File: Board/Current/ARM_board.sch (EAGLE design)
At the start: 168 parts, among them IC3 STM32F437VI, IC4 LM358DT, J1 USART/I2C, J10 ANALOG, J11 DGND, J12 DPWR, J13 DIGITAL, J14 SGND, J15 SPWR, J16 SERVO, J2 I2C2/USART3, J3 USART2, J5 SPI, J6 Bluesmirf, J7 SWD, J8 AGND, J9 APWR, Q1 STL4P2UH7, Q2 2STR1230, SW1 SW, U1 LSM330DLC, U10 BAV99, U11 BAV99, U12 USBLC6-2, U13 USBLC6-2, U14 STMPS2171MTR, U15 MC74HC164, U17 ?, U18 ?, U19 ?, U20 ?, U3 NC7SZU04, U4 L6206Q, U5 L6206Q, U6 SI7617, U7 SI7617, U8 SI7617, U9 SI7617, Y2 8MHz

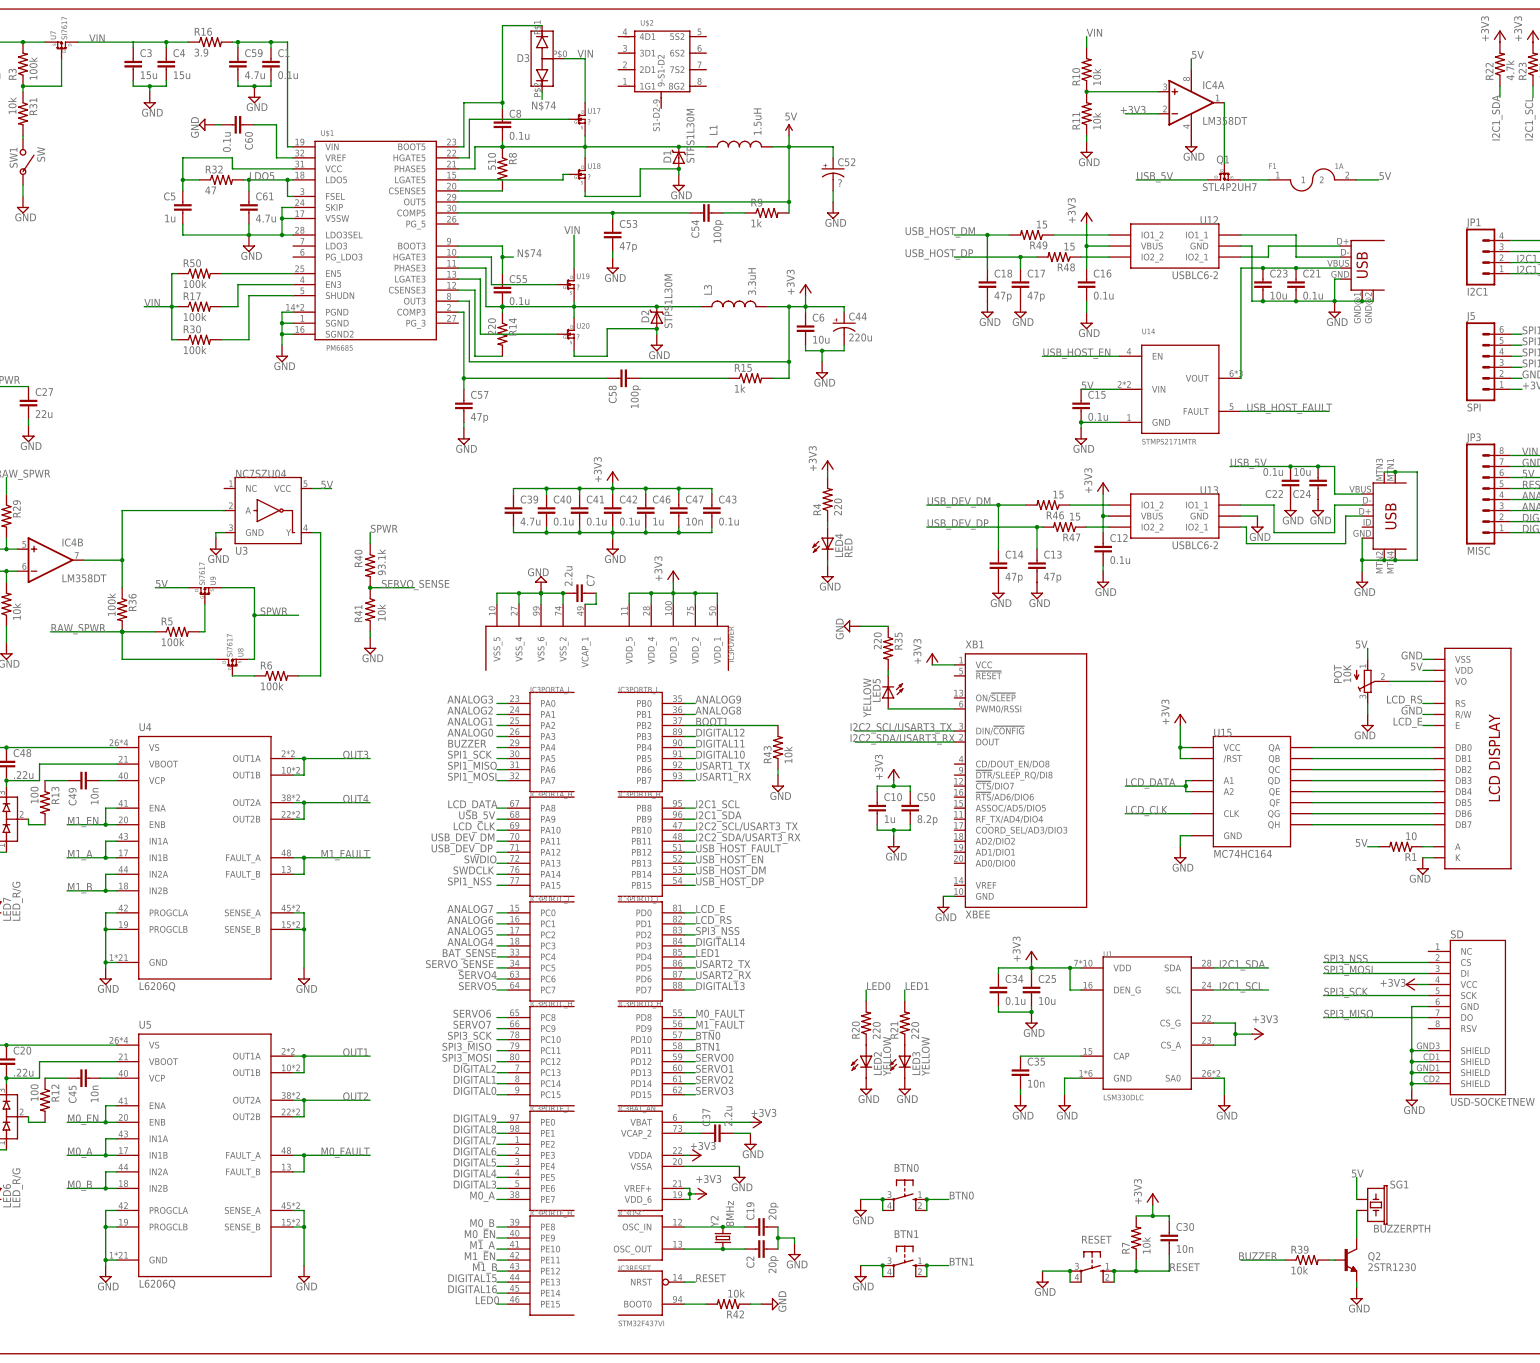
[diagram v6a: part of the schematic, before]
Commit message: Added more capacitors to entire schematic, including the remaining switching regulator capacitors.
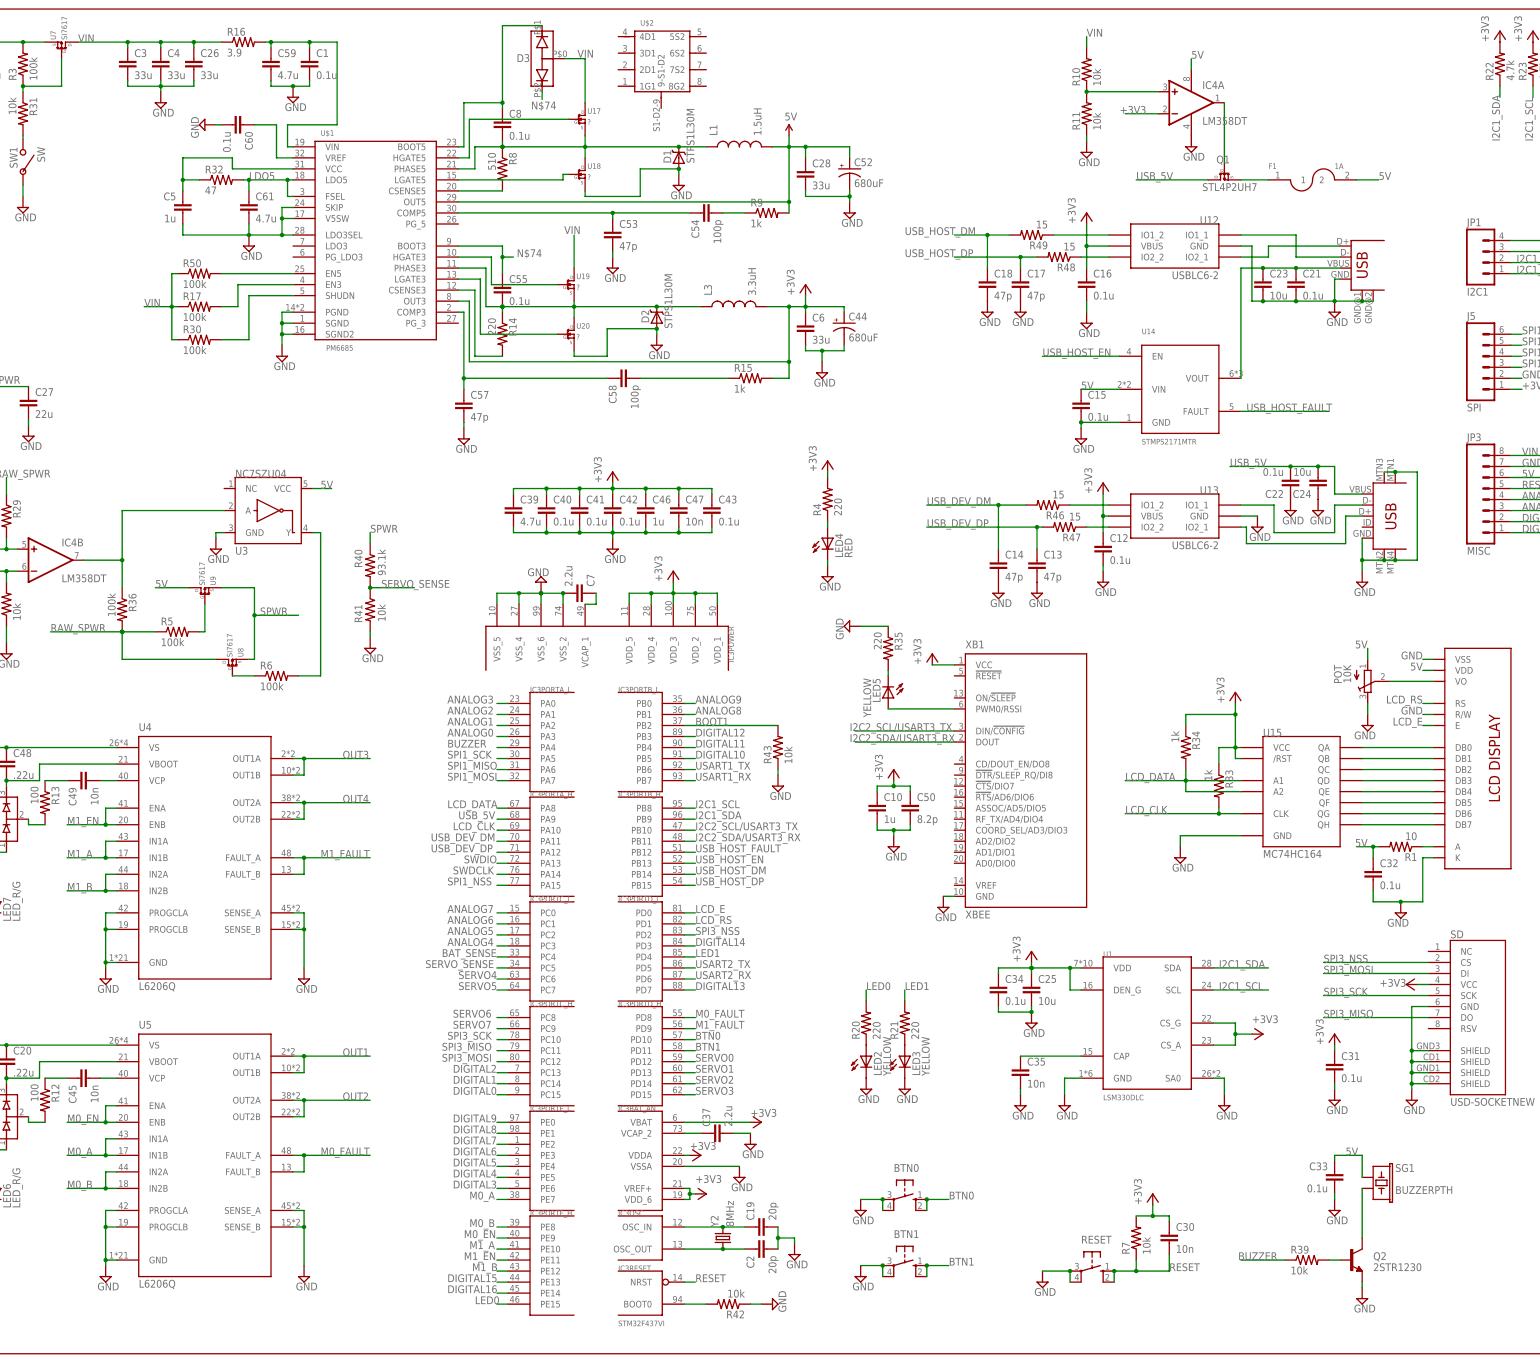
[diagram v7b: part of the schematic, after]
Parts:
- added C26: 33u, SparkFun:CAP0402-CAP
- added C28: 33u, SparkFun:CAP0603-CAP
- added C31, C32, C33: 0.1u, SparkFun:CAP0402-CAP
- added R33, R34: 1k, SparkFun:RESISTOR0402-RES
- C3, C4: value 15u -> 33u
- C44: value 220u -> 680uF
- C52: value ? -> 680uF
- C6: value 10u -> 33u
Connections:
- net +3V3: now also C31.1, R33.1, R34.1
- net 5V: now also C28.1, C32.1, C33.1
- net GND: now also C26.2, C28.2, C31.2, C32.2, C33.2
- net LCD_CLK: now also R33.2
- net LCD_DATA: now also R34.2
- net VIN: now also C26.1
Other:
- moved on the sheet: C1, C3, C4, C52, C59, Q2, R16, SG1, U15

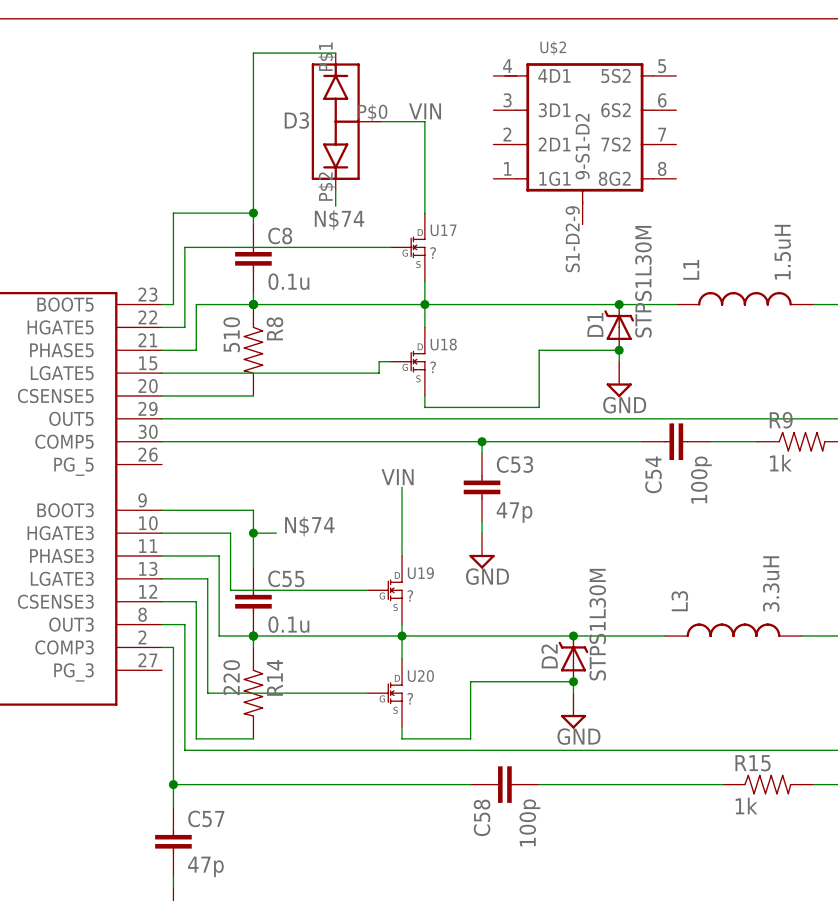
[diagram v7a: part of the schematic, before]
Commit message: Placed both of the dual mosfets on the schematic.
They replaced U17 & U18 were replaced with U17 (dual-mosfet).
They replaced U19 & U20 were replaced with U19 (dual-mosfet).
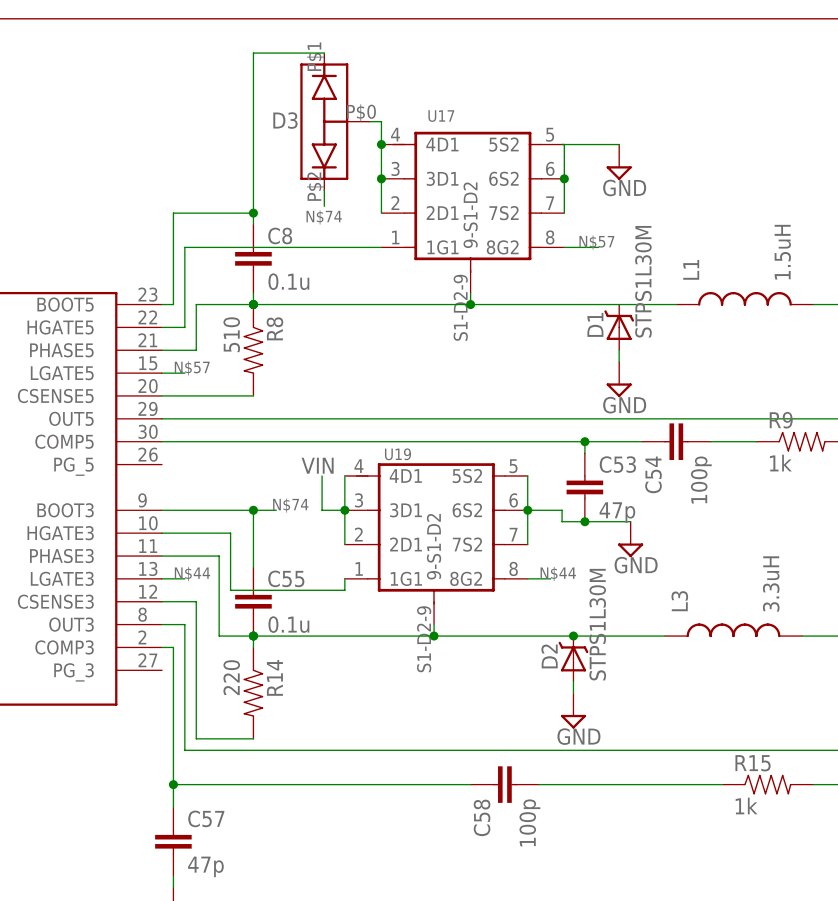
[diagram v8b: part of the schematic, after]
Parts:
- removed U$2: DUAL-MOSFET, r_cubed:DUAL-MOSFET
- removed U18, U20: ?, r_cubed:STL85N6F3
- U17, U19: value ? -> DUAL-MOSFET; device r_cubed:STL85N6F3 -> r_cubed:DUAL-MOSFET
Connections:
- removed net N$72: U$1.LGATE3, U20.G
- new net N$32: U19.5S2, U19.6S2, U19.7S2
- new net N$35: U17.5S2, U17.6S2, U17.7S2
- new net N$44: U$1.LGATE3, U19.8G2
- net GND: no longer U18.S, U20.S
- net N$56: now also U17.1G1; no longer U17.G
- net N$57: now also U17.8G2; no longer U18.G
- net N$66: now also U17.9-S1-D2; no longer U17.S, U18.D
- net N$73: now also U19.1G1; no longer U19.G
- net N$75: now also U19.9-S1-D2; no longer U19.S, U20.D
- net VIN: now also U17.2D1, U17.3D1, U17.4D1, U19.2D1, U19.3D1, U19.4D1; no longer U17.D, U19.D
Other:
- moved on the sheet: C53
